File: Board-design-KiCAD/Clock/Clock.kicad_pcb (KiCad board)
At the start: 2 copper layers, 27 parts, among them M1 SevSeg4Inch, M2 SevSeg4Inch, Y1 SevSeg1.8Inch, Y2 SevSeg1.8Inch, Y3 SevSeg1.8Inch, Y4 SevSeg1.8Inch

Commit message: Add new tracks
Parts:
- added 5V-Cin1: 0.22uF - 50V, Capacitor_THT:CP_Radial_D4.0mm_P2.00mm, F.Cu at (337.9, 385.5)
- added 5V-Cout1: 0.1uF - 50V, Capacitor_THT:CP_Radial_D5.0mm_P2.00mm, F.Cu at (331.8, 386.0)
- added 6V-Cin1: 0.33uF - 50V, Capacitor_THT:CP_Radial_D4.0mm_P2.00mm, F.Cu at (331.2, 392.1)
- added 6V-Cout1: 0.1uF - 50V, Capacitor_THT:CP_Radial_D5.0mm_P2.00mm, F.Cu at (345.1, 377.9)
- added CommonPinControl_YEAR1: ULN2003A, Package_DIP:DIP-16_W7.62mm_Socket_LongPads, F.Cu at (331.5, 354.7)
- added DATE_INPUT_CONTROL1: 74HC595, Package_DIP:DIP-16_W7.62mm_Socket_LongPads, F.Cu at (343.2, 354.7)
- added RDP1: 680, Resistor_THT:R_Axial_DIN0207_L6.3mm_D2.5mm_P10.16mm_Horizontal, F.Cu at (331.0, 376.7)
- added RDP2: 680, Resistor_THT:R_Axial_DIN0207_L6.3mm_D2.5mm_P10.16mm_Horizontal, F.Cu at (331.0, 380.7)
- added Regulator-5V1: LM7805_TO220, Package_TO_SOT_THT:TO-220-3_Horizontal_TabDown, F.Cu at (379.6, 372.8)
- added Regulator-6V1: L7806, Package_TO_SOT_THT:TO-220-3_Horizontal_TabDown, F.Cu at (391.2, 372.8)
- added TIME_INPUT_CONTROL1: 74HC595, Package_DIP:DIP-16_W7.62mm_Socket_LongPads, F.Cu at (355.0, 354.7)
- added YEAR_INPUT_CONTROL1: 74HC595, Package_DIP:DIP-16_W7.62mm_Socket_LongPads, F.Cu at (366.7, 354.7)
- BCD-TIME1: renamed from BCD-YEAR1; footprint Package_DIP:DIP-18_W7.62mm_LongPads -> Package_DIP:DIP-16_W7.62mm_Socket_LongPads
- CommonPinControl_TIME1: renamed from CommonPinControl1; footprint Package_DIP:DIP-18_W7.62mm_LongPads -> Package_DIP:DIP-16_W7.62mm_Socket_LongPads
- InputPowerConverter1: footprint Package_DIP:DIP-18_W7.62mm_LongPads -> Package_DIP:DIP-16_W7.62mm_Socket_LongPads
- renumbered BCD-TIME1 to BCD-YEAR1
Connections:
- net Net-(CommonPinControl1-Pad1) renamed EN_DIGIT_1
- net Net-(CommonPinControl1-Pad2) renamed EN_DIGIT_2
- net Net-(CommonPinControl1-Pad3) renamed EN_DIGIT_3
- net Net-(CommonPinControl1-Pad4) renamed EN_DIGIT_4
- net Net-(Y1-Pad1) renamed /Y1_EN
- net Net-(Y2-Pad1) renamed /Y2_EN
- net Net-(Y3-Pad1) renamed /Y3_EN
- net Net-(Y4-Pad1) renamed /Y4_EN
- BCD-TIME1 pad 16: Net-(BCD-YEAR1-Pad16) -> +6V
- BCD-TIME1 pad 3: Net-(BCD-YEAR1-Pad3) -> +5V
- BCD-TIME1 pad 4: Net-(BCD-YEAR1-Pad4) -> +5V
- BCD-TIME1 pad 5: Net-(BCD-YEAR1-Pad5) -> +5V
- BCD-YEAR1 pad 10: Net-(BCD-TIME1-Pad10) (its old number) -> /YEAR_D
- BCD-YEAR1 pad 11: Net-(BCD-TIME1-Pad11) (its old number) -> /YEAR_C
- BCD-YEAR1 pad 12: Net-(BCD-TIME1-Pad12) (its old number) -> /YEAR_B
- BCD-YEAR1 pad 13: Net-(BCD-TIME1-Pad13) (its old number) -> /YEAR_A
- BCD-YEAR1 pad 14: Net-(BCD-TIME1-Pad14) (its old number) -> /YEAR_G
- BCD-YEAR1 pad 15: Net-(BCD-TIME1-Pad15) (its old number) -> /YEAR_F
- BCD-YEAR1 pad 16: Net-(BCD-TIME1-Pad16) -> +6V
- BCD-YEAR1 pad 3: Net-(BCD-TIME1-Pad3) -> +5V
- BCD-YEAR1 pad 4: Net-(BCD-TIME1-Pad4) -> +5V
- BCD-YEAR1 pad 5: Net-(BCD-TIME1-Pad5) -> +5V
- BCD-YEAR1 pad 8: Net-(BCD-TIME1-Pad8) -> GND
- BCD-YEAR1 pad 9: Net-(BCD-TIME1-Pad9) (its old number) -> /YEAR_E
- CommonPinControl_TIME1 pad 12: Net-(CommonPinControl1-Pad12) -> /DP_EN
- CommonPinControl_TIME1 pad 13: Net-(CommonPinControl1-Pad13) -> /H4_EN
- CommonPinControl_TIME1 pad 14: Net-(CommonPinControl1-Pad14) -> /H3_EN
- CommonPinControl_TIME1 pad 15: Net-(CommonPinControl1-Pad15) -> /H2_EN
- CommonPinControl_TIME1 pad 16: Net-(CommonPinControl1-Pad16) -> /H1_EN
- H1 pad 1: Net-(H1-Pad1) -> /H1_EN
- H1 pad 8: Net-(H1-Pad1) -> /H1_EN
- H2 pad 1: Net-(H2-Pad1) -> /H2_EN
- H2 pad 8: Net-(H2-Pad1) -> /H2_EN
- M1 pad 1: Net-(M1-Pad1) -> /H3_EN
- M1 pad 8: Net-(M1-Pad1) -> /H3_EN
- M2 pad 1: Net-(M2-Pad1) -> /H4_EN
- M2 pad 8: Net-(M2-Pad1) -> /H4_EN
- Y1 pad 10: Net-(Y1-Pad10) -> /YEAR_G
- Y1 pad 2: Net-(Y1-Pad2) -> /YEAR_E
- Y1 pad 3: Net-(Y1-Pad3) -> /YEAR_D
- Y1 pad 4: Net-(Y1-Pad4) -> /YEAR_C
- Y1 pad 6: Net-(Y1-Pad6) -> /YEAR_B
- Y1 pad 7: Net-(Y1-Pad7) -> /YEAR_A
- Y1 pad 9: Net-(Y1-Pad9) -> /YEAR_F
- Y2 pad 10: Net-(Y2-Pad10) -> /YEAR_G
- Y2 pad 2: Net-(Y2-Pad2) -> /YEAR_E
- Y2 pad 3: Net-(Y2-Pad3) -> /YEAR_D
- Y2 pad 4: Net-(Y2-Pad4) -> /YEAR_C
- Y2 pad 6: Net-(Y2-Pad6) -> /YEAR_B
- Y2 pad 7: Net-(Y2-Pad7) -> /YEAR_A
- Y2 pad 9: Net-(Y2-Pad9) -> /YEAR_F
- Y3 pad 10: Net-(Y3-Pad10) -> /YEAR_G
- Y3 pad 2: Net-(Y3-Pad2) -> /YEAR_E
- Y3 pad 3: Net-(Y3-Pad3) -> /YEAR_D
- Y3 pad 4: Net-(Y3-Pad4) -> /YEAR_C
- Y3 pad 6: Net-(Y3-Pad6) -> /YEAR_B
- Y3 pad 7: Net-(Y3-Pad7) -> /YEAR_A
- Y3 pad 9: Net-(Y3-Pad9) -> /YEAR_F
- Y4 pad 10: Net-(Y4-Pad10) -> /YEAR_G
- Y4 pad 2: Net-(Y4-Pad2) -> /YEAR_E
- Y4 pad 3: Net-(Y4-Pad3) -> /YEAR_D
- Y4 pad 4: Net-(Y4-Pad4) -> /YEAR_C
- Y4 pad 6: Net-(Y4-Pad6) -> /YEAR_B
- Y4 pad 7: Net-(Y4-Pad7) -> /YEAR_A
- Y4 pad 9: Net-(Y4-Pad9) -> /YEAR_F

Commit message: Add some display wirings
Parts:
- removed BCD-DATE1, BCD-YEAR1: 74LS47, Package_DIP:DIP-18_W7.62mm_LongPads
- removed CommonPinControl_YEAR1: ULN2003A, Package_DIP:DIP-16_W7.62mm_Socket_LongPads
- removed D1, D2, Mo1, Mo2: SevSeg1.8Inch, Custom:SevSeg1.8Inch
- removed DATE_INPUT_CONTROL1, YEAR_INPUT_CONTROL1: 74HC595, Package_DIP:DIP-16_W7.62mm_Socket_LongPads
- added Da_1: SevSeg1.8Inch, Custom:SevSeg1.8Inch, F.Cu at (426.0, 278.0)
- added Da_2: SevSeg1.8Inch, Custom:SevSeg1.8Inch, F.Cu at (464.5, 278.0)
- added INVERTER_1: 74HC14, Package_DIP:DIP-14_W7.62mm_Socket_LongPads, B.Cu at (367.1, 194.7)
- added INVERTER_2: 74HC14, Package_DIP:DIP-14_W7.62mm_Socket_LongPads, B.Cu at (379.8, 162.4)
- added Mo_1: SevSeg1.8Inch, Custom:SevSeg1.8Inch, F.Cu at (503.0, 278.0)
- added Mo_2: SevSeg1.8Inch, Custom:SevSeg1.8Inch, F.Cu at (541.5, 278.0)
- BCD-TIME1, CommonPinControl_TIME1, InputPowerConverter1, RDP1, RDP2, TIME_INPUT_CONTROL1: moved to B.Cu
- moved Y2 297.1 mm to (253.0, 97.0)
- moved Y1 297.0 mm to (214.5, 97.0)
- moved RDP2 256.4 mm to (413.4, 137.9), turned to 270 degrees
- moved CommonPinControl_TIME1 254.2 mm to (380.2, 148.2), turned to 90 degrees
- moved Y4 241.1 mm to (330.0, 97.0)
- moved Y3 241.0 mm to (291.6, 97.0)
- moved InputPowerConverter1 207.2 mm to (382.9, 194.7)
- moved BCD-TIME1 169.3 mm to (344.4, 194.7)
- moved TIME_INPUT_CONTROL1 164.6 mm to (316.6, 194.7)
- moved Regulator-5V1 154.0 mm to (268.4, 266.4), turned to 180 degrees
- moved Regulator-6V1 152.9 mm to (281.4, 266.4), turned to 180 degrees
- moved 6V-Cin1 147.4 mm to (255.2, 265.8), turned to 270 degrees
- moved 5V-Cin1 138.4 mm to (255.3, 274.4), turned to 270 degrees
- moved RDP1 136.5 mm to (347.1, 241.1)
- moved 6V-Cout1 124.8 mm to (289.0, 266.4), turned to 270 degrees
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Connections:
- net Net-(CommonPinControl_TIME1-Pad5) renamed DP_PWM
- net Net-(TIME_INPUT_CONTROL1-Pad11) renamed CLOCK
- net Net-(TIME_INPUT_CONTROL1-Pad12) renamed LATCH
- net Net-(TIME_INPUT_CONTROL1-Pad14) renamed TIME_DATA_INPUT
- BCD-TIME1 pad 10: Net-(BCD-TIME1-Pad10) -> SIGNAL_TIME_D
- BCD-TIME1 pad 11: Net-(BCD-TIME1-Pad11) -> SIGNAL_TIME_C
- BCD-TIME1 pad 12: Net-(BCD-TIME1-Pad12) -> SIGNAL_TIME_B
- BCD-TIME1 pad 13: Net-(BCD-TIME1-Pad13) -> SIGNAL_TIME_A
- BCD-TIME1 pad 14: Net-(BCD-TIME1-Pad14) -> SIGNAL_TIME_G
- BCD-TIME1 pad 15: Net-(BCD-TIME1-Pad15) -> SIGNAL_TIME_F
- BCD-TIME1 pad 16: +6V -> +5V
- BCD-TIME1 pad 9: Net-(BCD-TIME1-Pad9) -> SIGNAL_TIME_E
- CommonPinControl_TIME1 pad 1: EN_DIGIT_1 -> Net-(CommonPinControl_TIME1-Pad1)
- CommonPinControl_TIME1 pad 2: EN_DIGIT_2 -> Net-(CommonPinControl_TIME1-Pad2)
- CommonPinControl_TIME1 pad 3: EN_DIGIT_3 -> Net-(CommonPinControl_TIME1-Pad3)
- CommonPinControl_TIME1 pad 4: EN_DIGIT_4 -> Net-(CommonPinControl_TIME1-Pad4)
- InputPowerConverter1 pad 1: Net-(BCD-TIME1-Pad13) -> PWR_TIME_A
- InputPowerConverter1 pad 2: Net-(BCD-TIME1-Pad12) -> PWR_TIME_B
- InputPowerConverter1 pad 3: Net-(BCD-TIME1-Pad11) -> PWR_TIME_C
- InputPowerConverter1 pad 4: Net-(BCD-TIME1-Pad10) -> PWR_TIME_D
- InputPowerConverter1 pad 5: Net-(BCD-TIME1-Pad9) -> PWR_TIME_E
- InputPowerConverter1 pad 6: Net-(BCD-TIME1-Pad15) -> PWR_TIME_F
- InputPowerConverter1 pad 7: Net-(BCD-TIME1-Pad14) -> PWR_TIME_G
- TIME_INPUT_CONTROL1 pad 10: Net-(TIME_INPUT_CONTROL1-Pad10) -> +5V
- TIME_INPUT_CONTROL1 pad 13: Net-(TIME_INPUT_CONTROL1-Pad13) -> GND
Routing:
- net /TIME_G: track 883.6 -> 468.2 mm, vias 0 -> 2
- net /TIME_E: track 0.00 -> 367.1 mm
- net /TIME_C: track 0.00 -> 358.2 mm, vias 0 -> 1
- net /TIME_D: track 0.00 -> 350.4 mm, vias 0 -> 1
- net /H1_EN: track 0.00 -> 327.1 mm, vias 0 -> 2
- net GND: track 120.2 -> 419.3 mm, vias 0 -> 2
- net +5V: track 0.00 -> 280.3 mm, vias 0 -> 5
- net /H4_EN: track 0.00 -> 276.4 mm
- net +11V: track 28.6 -> 280.3 mm, vias 0 -> 5
- net /YEAR_B: track 0.00 -> 198.9 mm
- net /H3_EN: track 0.00 -> 190.6 mm
- net /DATE_B: track 0.00 -> 186.2 mm
- net /DATE_D: track 0.00 -> 179.9 mm
- net /YEAR_D: track 0.00 -> 177.2 mm
- net /DP_EN: track 0.00 -> 176.4 mm, vias 0 -> 4
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
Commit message: Finish display wirings
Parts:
- added BCD-DATE1: 74LS47, Package_DIP:DIP-18_W7.62mm_LongPads, B.Cu at (396.5, 289.0)
- added BCD-YEAR1: 74LS47, Package_DIP:DIP-18_W7.62mm_LongPads, B.Cu at (360.8, 87.2)
- added CommonPinControl_DATE1: ULN2003A, Package_DIP:DIP-16_W7.62mm_Socket_LongPads, B.Cu at (367.0, 289.0)
- added CommonPinControl_YEAR1: ULN2003A, Package_DIP:DIP-16_W7.62mm_Socket_LongPads, B.Cu at (410.8, 105.5)
- added DATE_INPUT_CONTROL1: 74HC595, Package_DIP:DIP-16_W7.62mm_Socket_LongPads, B.Cu at (345.8, 288.8)
- added YEAR_INPUT_CONTROL1: 74HC595, Package_DIP:DIP-16_W7.62mm_Socket_LongPads, B.Cu at (379.0, 105.0)
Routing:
- net GND: track 419.3 -> 1183.0 mm, vias 2 -> 4
- net +6V: track 25.0 -> 680.0 mm, vias 0 -> 4
- net EN_DIGIT_3: track 0.00 -> 504.4 mm, vias 0 -> 14
- net CLOCK: track 0.00 -> 463.7 mm, vias 0 -> 6
- net EN_DIGIT_4: track 0.00 -> 462.8 mm, vias 0 -> 8
- net +5V: track 280.3 -> 647.8 mm, vias 5 -> 7
- net EN_DIGIT_1: track 0.00 -> 346.3 mm, vias 0 -> 10
- net LATCH: track 0.00 -> 324.9 mm, vias 0 -> 3
- net +11V: track 280.3 -> 603.4 mm, vias 5 -> 7
- net EN_DIGIT_2: track 0.00 -> 263.3 mm, vias 0 -> 6
- net /Y1_EN: track 27.6 -> 233.0 mm, vias 0 -> 1
- net /Y2_EN: track 30.5 -> 217.9 mm, vias 0 -> 1
- net /Mo2_EN: track 30.6 -> 205.3 mm
- net /Y3_EN: track 31.5 -> 177.6 mm
- net Net-(BCD-DATE1-Pad6): track 0.00 -> 133.5 mm
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
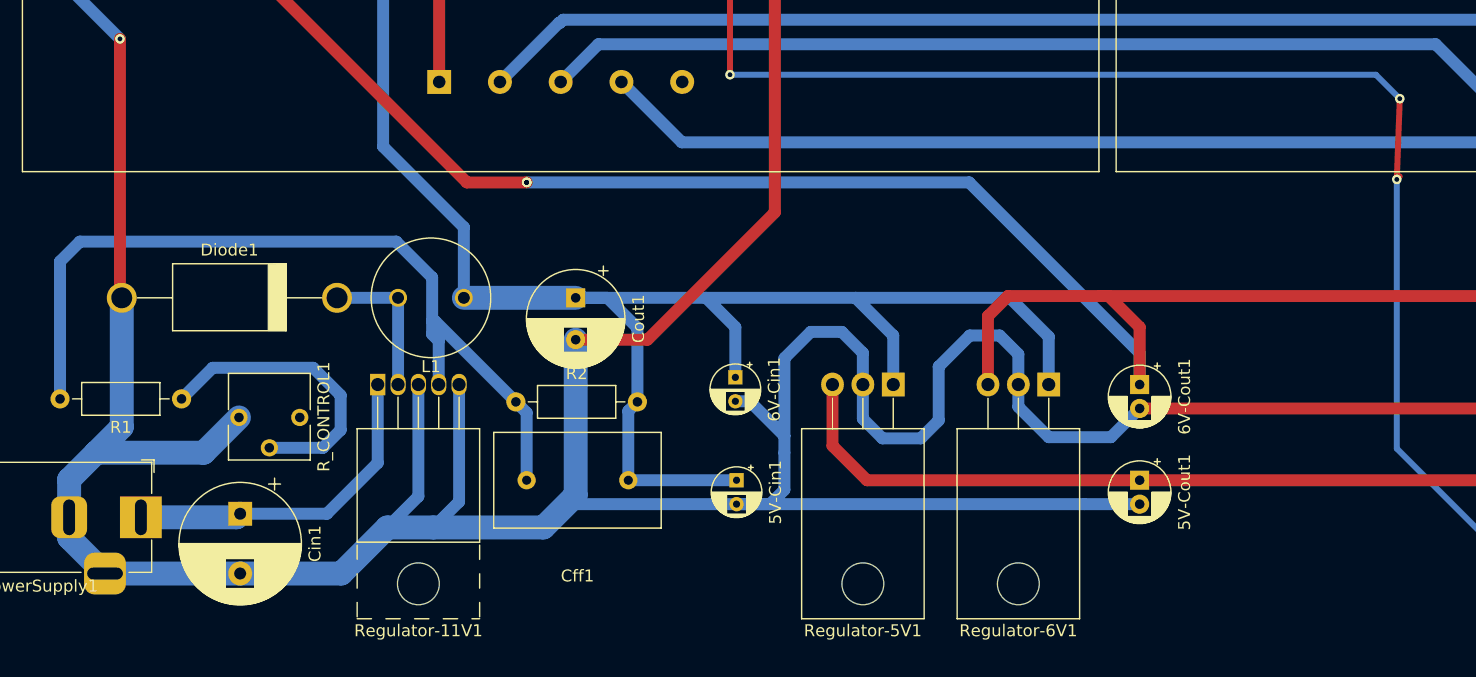
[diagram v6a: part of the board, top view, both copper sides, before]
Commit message: Rearrange some minor components
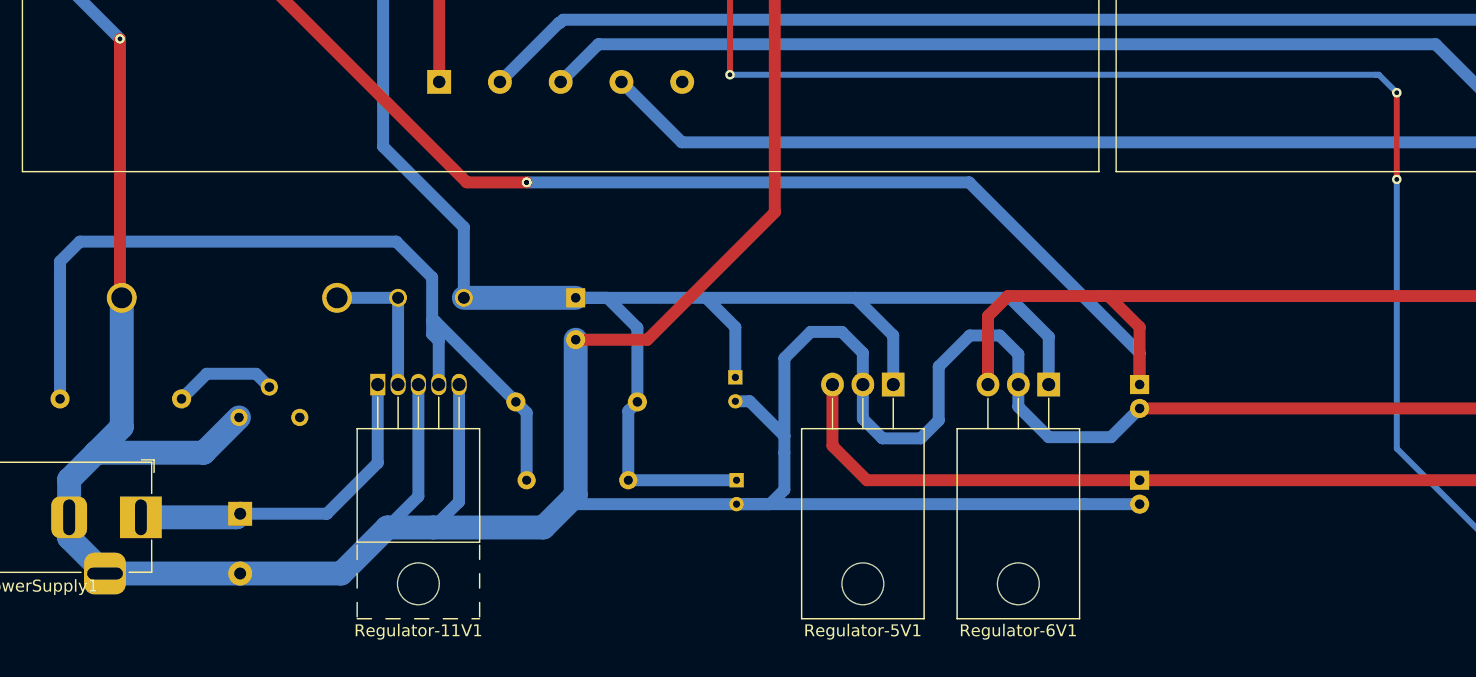
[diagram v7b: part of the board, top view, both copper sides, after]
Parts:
- 5V-Cin1, 5V-Cout1, 6V-Cin1, 6V-Cout1, Cff1, Cin1, Cout1, Diode1, L1, R1, R2, R_CONTROL1: moved to B.Cu
- turned R_CONTROL1 to 90 degrees
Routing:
- net Net-(R1-Pad1): track 24.8 -> 8.67 mm

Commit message: Add Blue Pill footprint on PCB design and perform existing wirings
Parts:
- added MCU_1: STM32F103CxT6-BluePill, Custom:STM32F103CxT6-BluePill, B.Cu at (485.0, 96.2)
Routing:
- net DATE_DATA_INPUT: track 0.00 -> 461.1 mm, vias 0 -> 4
- net EN_DIGIT_1: track 346.3 -> 648.5 mm
- net TIME_DATA_INPUT: track 0.00 -> 283.5 mm, vias 0 -> 7
- net EN_DIGIT_4: track 462.8 -> 732.6 mm
- net GND: track 1183.0 -> 1372.8 mm
- net CLOCK: track 463.7 -> 632.1 mm, vias 6 -> 17
- net DP_PWM: track 0.00 -> 146.3 mm, vias 0 -> 8
- net YEAR_DATA_INPUT: track 0.00 -> 129.4 mm, vias 0 -> 1
- net EN_DIGIT_2: track 263.3 -> 391.7 mm, vias 6 -> 8
- net LATCH: track 324.9 -> 447.6 mm, vias 3 -> 8
- net EN_DIGIT_3: track 504.0 -> 587.9 mm, vias 14 -> 15
- net +5V: track 647.8 -> 704.6 mm
- net /H4_EN: track 281.2 -> 280.4 mm
